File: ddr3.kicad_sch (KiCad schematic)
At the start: 61 parts, among them U7 AS4C256M16D3, U8 TPS51200DRCT

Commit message: [#68236] Update symbols and footprints, clean ERC and DRC
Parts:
- C42, C44, C46, C57, C62, C63: Public (none) -> False
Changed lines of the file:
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@@
+      (effects (font (size 1.27 1.27)) (justify left bottom) hide)
+    )
+    (property "Public" "False" (at 285.75 38.1 0)
       (effects (font (size 1.27 1.27)) (justify left bottom) hide)
     )
@@
     )
     (property "Dielectric" "" (at 274.32 38.1 0)
+      (effects (font (size 1.27 1.27)) (justify left bottom) hide)
+    )
+    (property "Public" "False" (at 276.86 38.1 0)
       (effects (font (size 1.27 1.27)) (justify left bottom) hide)
     )
@@
       (effects (font (size 1.27 1.27)) (justify left bottom) hide)
     )
+    (property "Public" "False" (at 147.32 208.28 0)
+      (effects (font (size 1.27 1.27)) (justify left bottom) hide)
+    )
     (pin "1")
     (pin "2")
@@
       (effects (font (size 1.27 1.27)) (justify left bottom) hide)
     )
+    (property "Public" "False" (at 137.16 198.12 0)
+      (effects (font (size 1.27 1.27)) (justify left bottom) hide)
+    )
     (pin "1")
     (pin "2")
@@
       (effects (font (size 1.27 1.27)) (justify left bottom) hide)
     )
+    (property "Public" "False" (at 129.54 198.12 0)
+      (effects (font (size 1.27 1.27)) (justify left bottom) hide)
+    )
     (pin "1")
     (pin "2")
@@
       (effects (font (size 1.27 1.27)) (justify left bottom) hide)
     )
+    (property "Public" "False" (at 81.28 113.03 0)
+      (effects (font (size 1.27 1.27)) (justify left bottom) hide)
+    )

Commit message: [#82378] Project refresh 81589
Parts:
- R100, R162, R163, R164, R167, R168, R169, R170, R171, R172, R173, R174, R175, R176, R177, R178, R179, R180, R181, R182, R183, R184, R54, R55, R56, R99: DNP DNP -> (none)
- U7: footprint antmicro-footprints:BGA-96_9.0x13.0mm_Layout2x3x16_P0.8mm -> antmicro-footprints:BGA-96-48_7.5x13.5mm_Layout9x16_P0.8mm; MPN AS4C256M16D3 -> AS4C256M16D3LC-12BCN
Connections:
- net at U7.J1 (NC): now also U7.J9 (NC), U7.L1 (NC), U7.L9 (NC), U7.M7 (NC)
- no-connect marks 5 -> 0

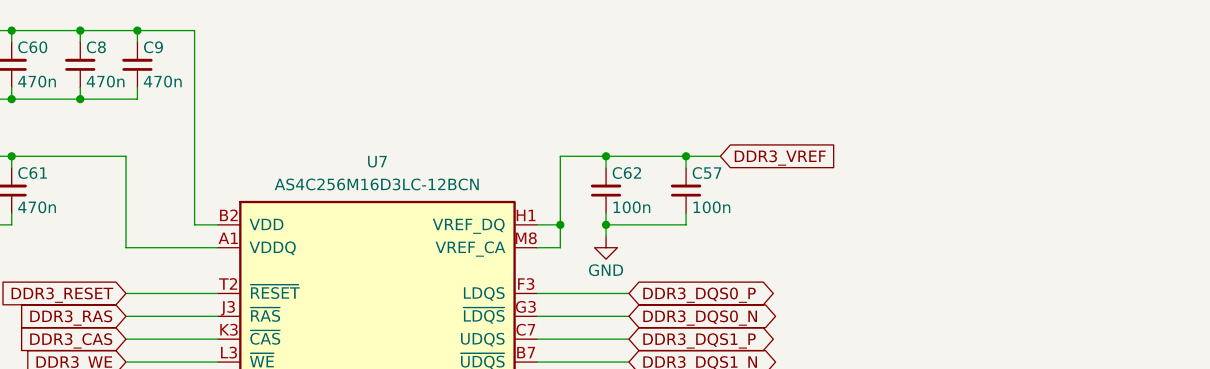
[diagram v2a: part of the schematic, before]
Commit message: started routing the ddr3 memory for defined stackup from Multi CB
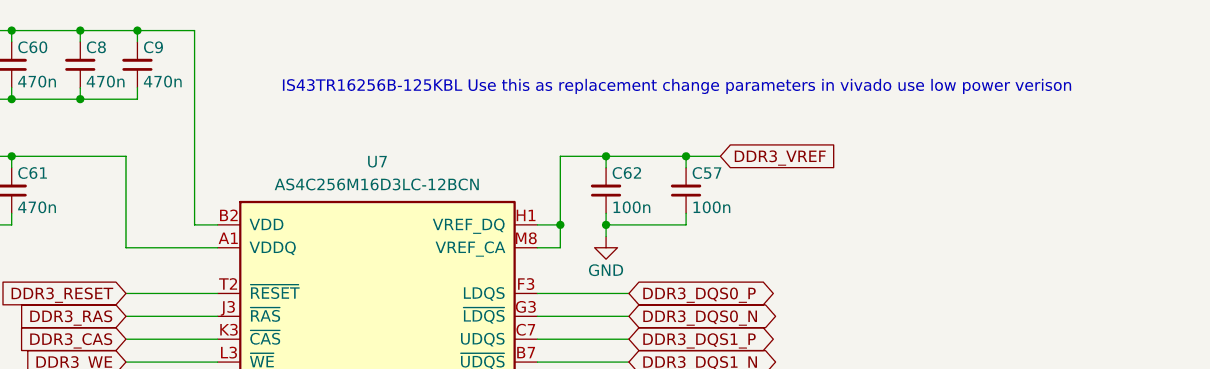
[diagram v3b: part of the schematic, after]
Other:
- note added: "IS43TR16256B-125KBL Use this as replacement change parameters in vivado use low power verison"

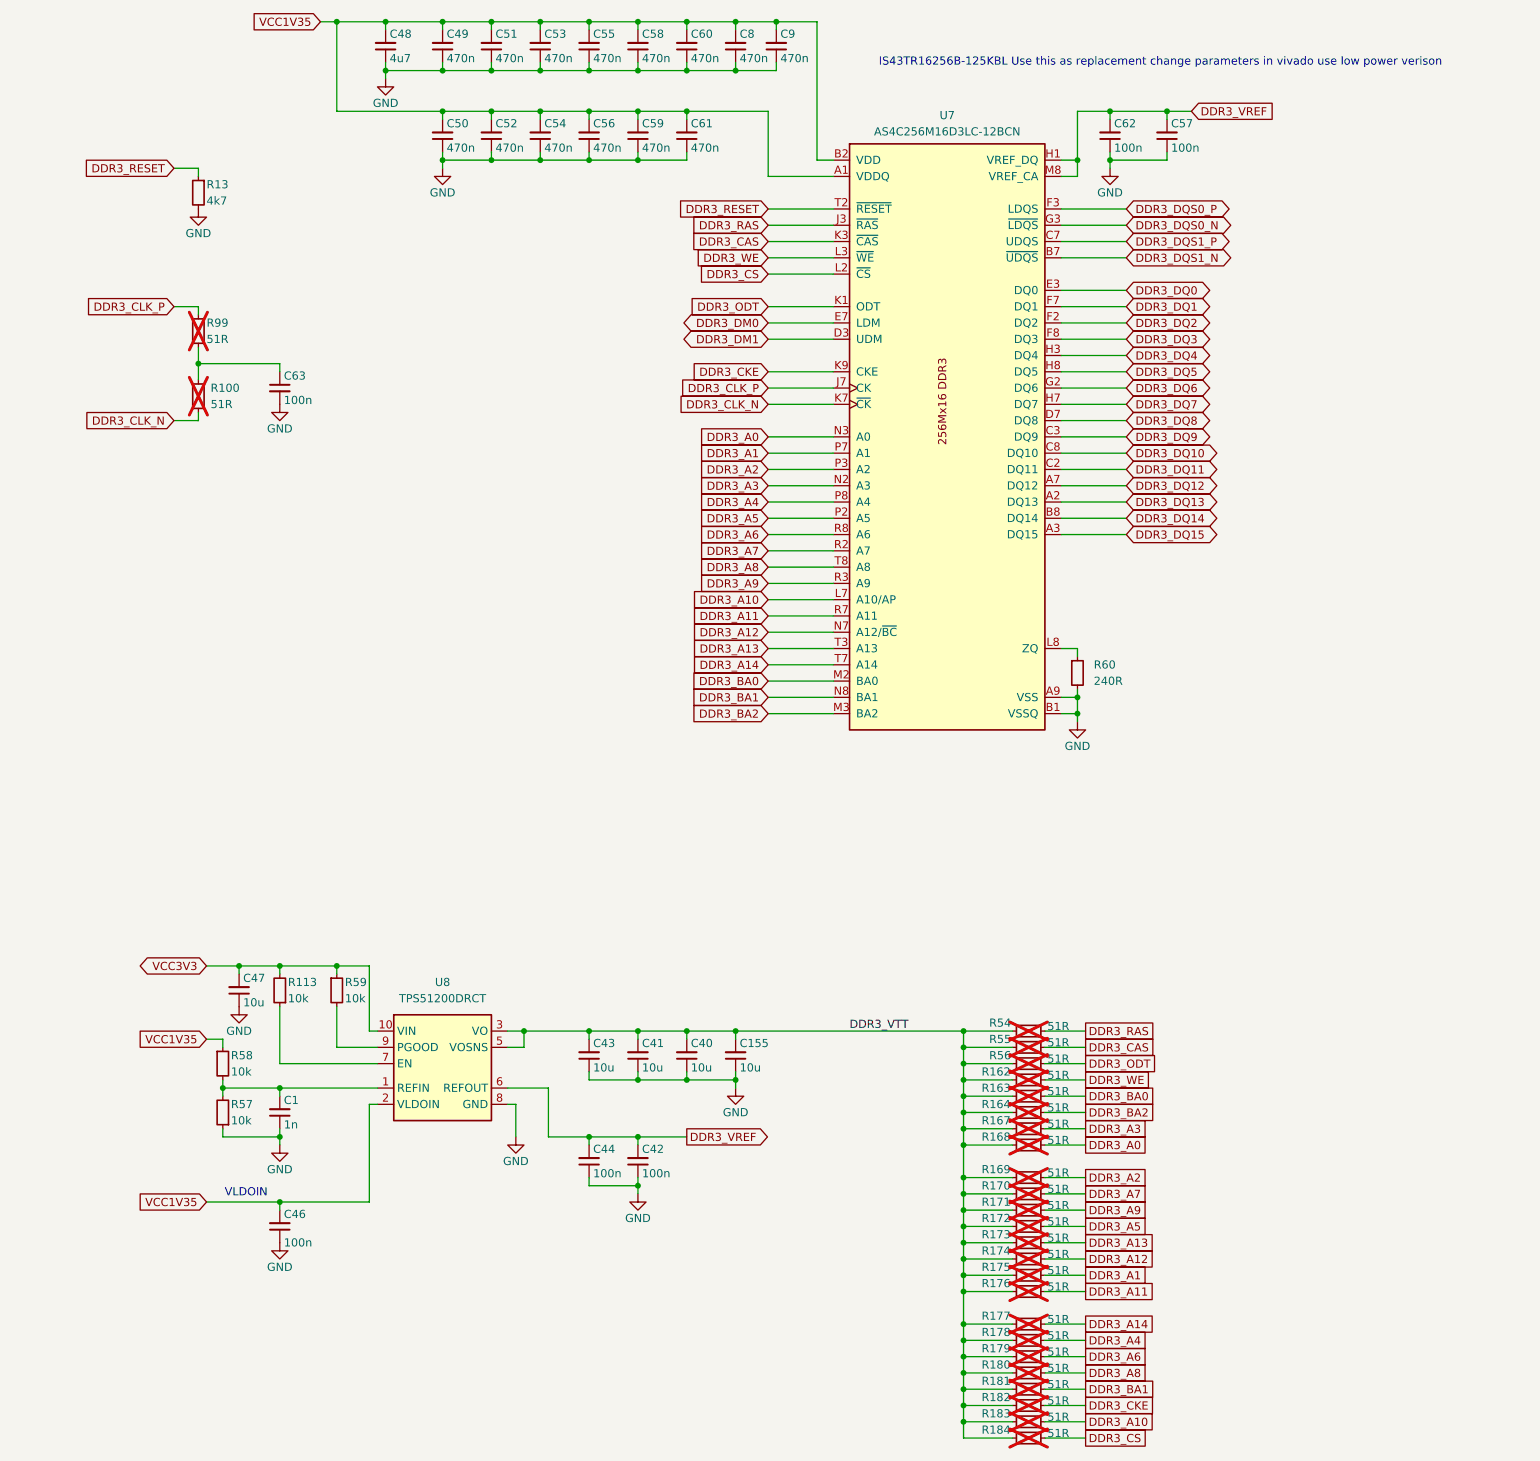
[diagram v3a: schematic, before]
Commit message: fix: add history files to gitignore
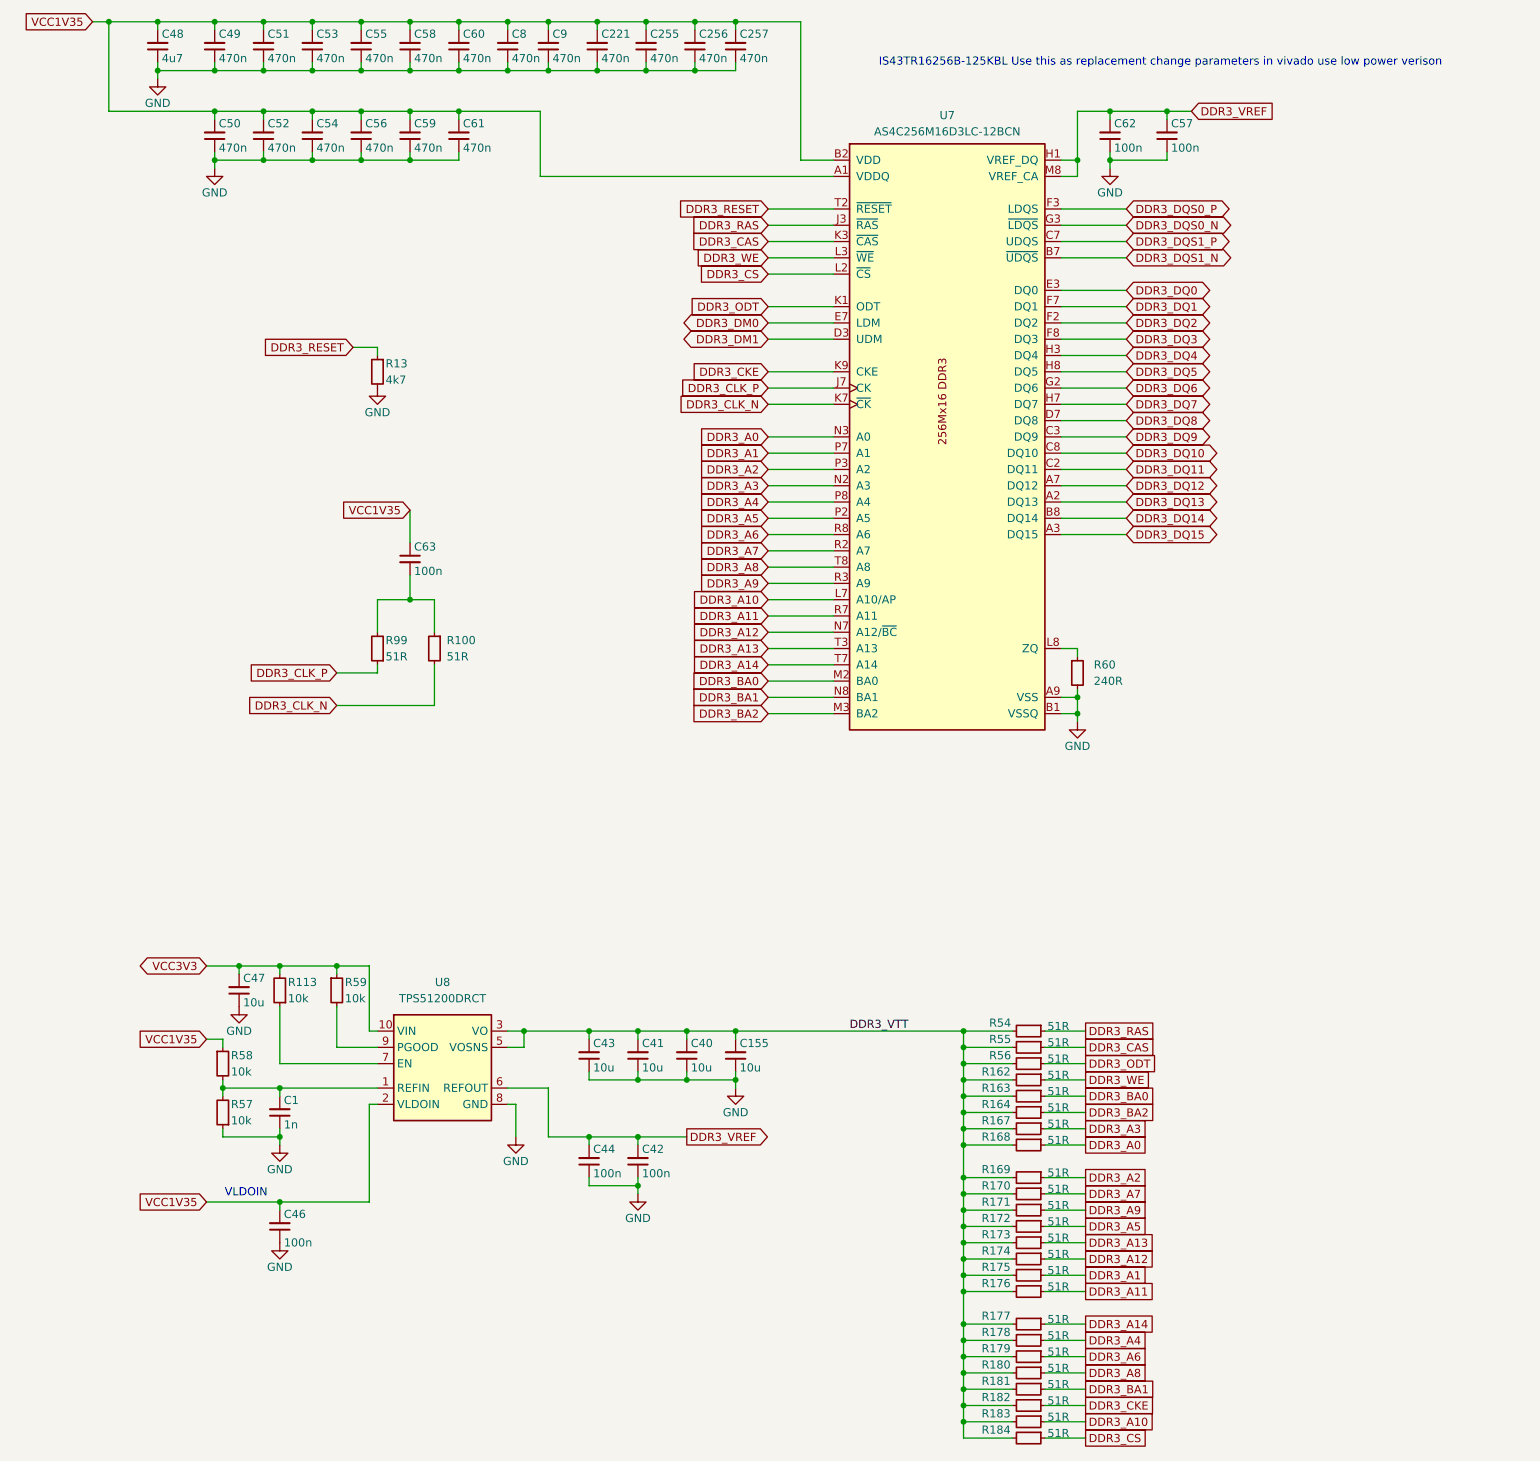
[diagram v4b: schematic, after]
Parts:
- added C221, C255, C256, C257: C_470n_0402, Capacitor_SMD:C_0402_1005Metric, symbol antmicroCapacitors0402:C_470n_0402
- C48: footprint antmicro-footprints:C_0402_1005Metric -> Capacitor_SMD:C_0402_1005Metric
- R100, R162, R163, R164, R167, R168, R169, R170, R171, R172, R173, R174, R175, R176, R177, R178, R179, R180, R181, R182, R183, R184, R54, R55, R56, R99: now fitted; now in the parts list
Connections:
- net DDR3_CLK_P: now also R99.1; no longer R99.2
- net GND: now also C221.1, C255.1, C256.1, C257.1; no longer C63.2
- net VCC1V35: now also C63.1, C221.2, C255.2, C256.2, C257.2
- new net: C63.2, R100.1, R99.2
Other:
- moved on the sheet: C48, C49, C50, C51, C52, C53, C54, C55, C56, C58, C59, C60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
